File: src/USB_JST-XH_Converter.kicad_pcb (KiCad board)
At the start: 2 copper layers, 55.9 x 35.9 mm, 48 parts, among them SW1 SS-12D00G3, SW2 SML-E12V8WT86, U1 TCKE805NAWSON10B_TOS-REC, U2 TLP293

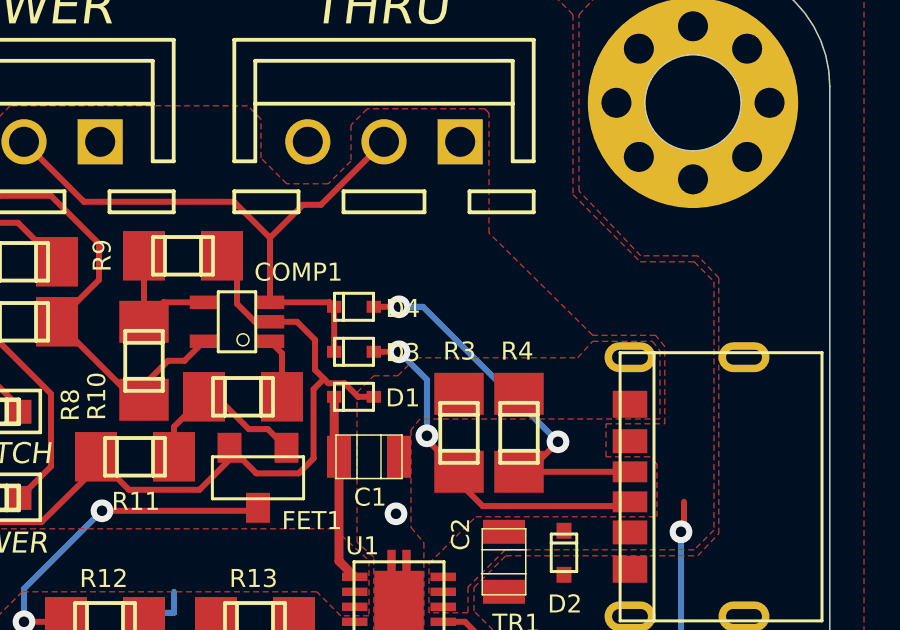
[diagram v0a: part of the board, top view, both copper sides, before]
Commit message: 3Aモード用LEDの追加
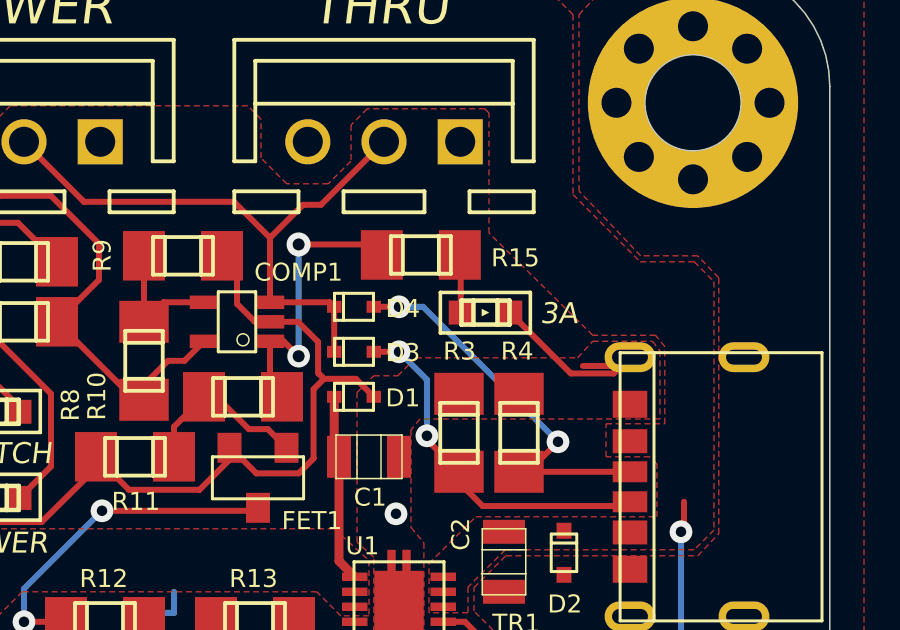
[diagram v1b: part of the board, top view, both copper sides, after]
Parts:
- added R10: 10, USB_JST-XH_Converter:RG2012, F.Cu at (161.5, 96.7)
- added SW2: SML-E12V8WT86, USB_JST-XH_Converter:SML-E12V8WT86, F.Cu at (165.8, 98.6)
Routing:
- net Net-(COMP1-PadOUT): track 2.02 -> 9.82 mm, vias 0 -> 2
- net GND: track 39.7 -> 46.4 mm
- net (no net): track 0.00 -> 1.93 mm
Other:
- board text added: "3A"
- board text added: "R15"

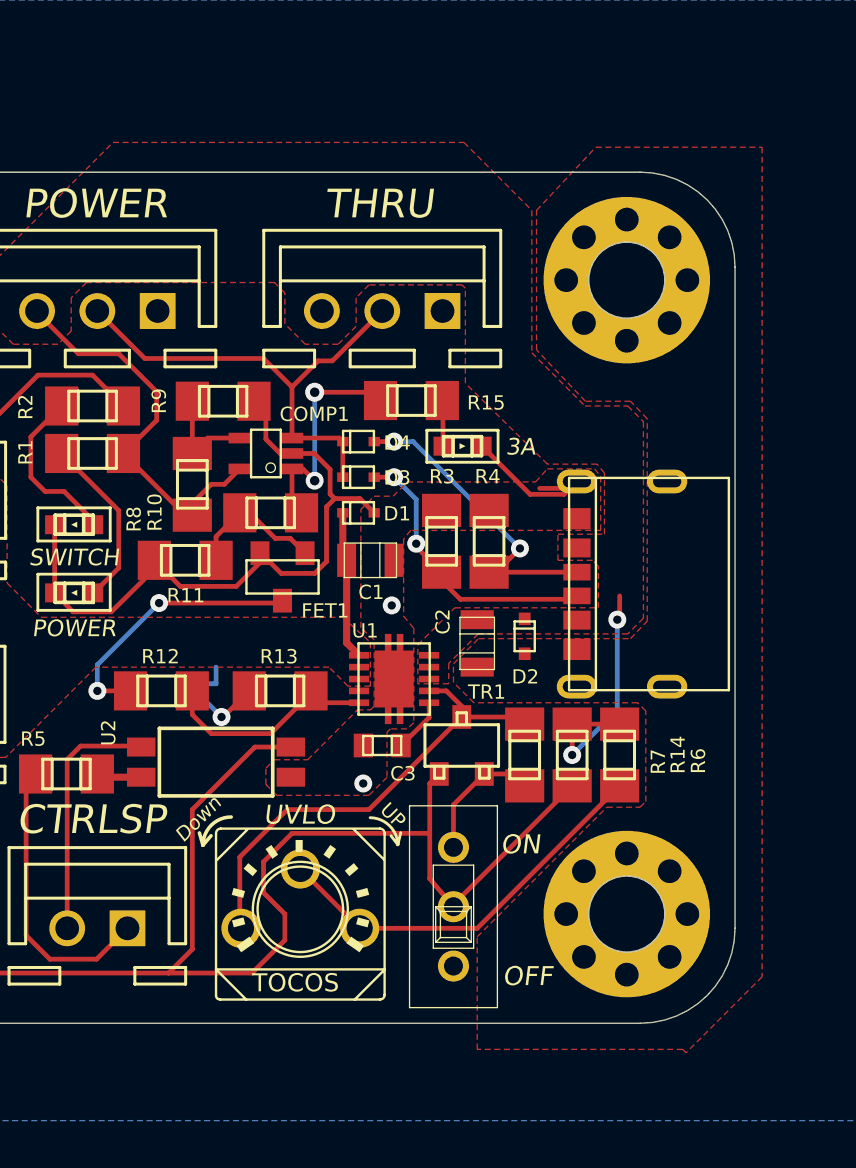
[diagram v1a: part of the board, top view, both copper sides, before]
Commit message: 微修正、BJTのBS間抵抗の追加
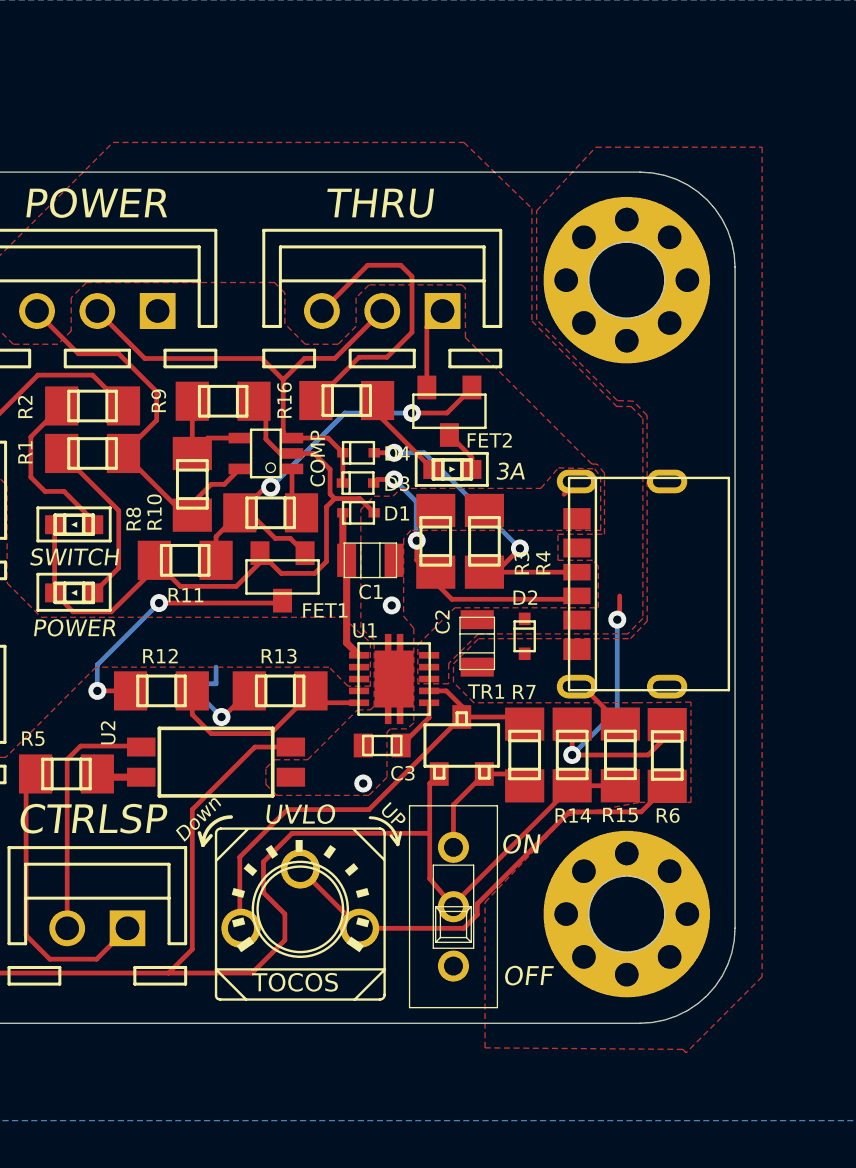
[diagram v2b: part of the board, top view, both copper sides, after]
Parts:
- removed R10 (x2): 10, USB_JST-XH_Converter:RG2012
- removed R11: 10k, USB_JST-XH_Converter:RG2012
- removed the SW2 at (165.8, 98.6)
- added FET2: BSS138, USB_JST-XH_Converter:SOT-23, F.Cu at (164.4, 96.2)
- added LED1: SML-E12V8WT86, USB_JST-XH_Converter:SML-E12V8WT86, F.Cu at (165.3, 99.6)
- added R12: 10, USB_JST-XH_Converter:RG2012, F.Cu at (155.6, 101.4)
- added R13: 10k, USB_JST-XH_Converter:RG2012, F.Cu at (154.6, 103.4)
- added R16: 100k, USB_JST-XH_Converter:RG2012, F.Cu at (171.6, 112.9)
- added R18: 100, USB_JST-XH_Converter:RG2012, F.Cu at (158.8, 96.7)
- moved R6 2.00 mm to (173.6, 113.0)
- moved D4 0.47 mm to (160.6, 98.9)
- moved D3 0.25 mm to (160.6, 100.2)
- moved R3 0.25 mm to (163.8, 103.9)
- moved R4 0.20 mm to (165.9, 103.9)
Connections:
- FET1 pad G: Net-(FET1-PadG) -> OUT
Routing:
- net OUT: track 0.00 -> 17.8 mm, vias 0 -> 2
- net VCC_P: track 28.3 -> 43.7 mm
- net Net-(COMP1-PadOUT): track 9.82 -> 2.02 mm, vias 2 -> 0
- net Net-(FET1-PadG): track 5.87 -> 0.00 mm
- net Net-(LED1-PadA): track 0.00 -> 4.14 mm
- net Net-(R6-PadLEFT): track 17.0 -> 19.2 mm
- net SWITCH: track 74.9 -> 77.0 mm
- net (no net): track 1.93 -> 0.00 mm
- net Net-(FET2-PadD): track 0.00 -> 1.87 mm
- net CC1: track 12.4 -> 13.2 mm
- net GND: track 46.4 -> 47.0 mm
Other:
- board text added: "COMP"
- board text added: "FET2"
- board text added: "R16"
- board text removed: "COMP1"
